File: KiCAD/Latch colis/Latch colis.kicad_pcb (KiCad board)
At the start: 2 copper layers, 140.8 x 44.7 mm, 12 parts, among them J1 KF301-2P, J2 KF301-2P, J3 KF301-2P, J4 Jauges, K1 Relay_SPDT, K2 Relay_SPDT, Q1 2N2222A, U1 Heltec_LoRa32_V2_RST_side, U2 Module HX711

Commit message: Passage au reveil par minuterie RTC, bibliotheques KiCad partagees, outils MCP
- Firmware courrier_emetteur : reveil profond par minuterie RTC au lieu du
  contact de porte, tarage HX711 persistant en memoire RTC, notification
  sans distinction nouveau/ancien courrier
- Variante "Latch colis sans inter" du schema KiCad, empreintes partagees
  (fp-lib-table) et PDF de brochage Heltec ajoutes
- Registre de travail (TODO.md) et espace de travail VS Code multi-dossiers
- Mise en place des serveurs MCP (Context7, Firecrawl, KiCad) avec script
  d'installation reutilisable sur une nouvelle machine (MCP-SETUP.md,
  setup-mcp-tools.ps1)

Co-Authored-By: Claude Sonnet 5 <noreply@anthropic.com>
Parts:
- Q1: footprint Package_TO_SOT_THT:TO-92 -> Package_TO_SOT_THT:TO-92L_Inline_Wide
- R1: value R -> 1k
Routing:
- net GND: track 166.6 -> 169.5 mm
- net Net-(Q1-Pad2): track 6.14 -> 8.73 mm
- net Net-(D1-K): track 189.7 -> 191.4 mm
- net Net-(U1-13): track 39.3 -> 41.0 mm
- net Net-(J2-Pad1): track 37.5 -> 36.3 mm
- net Net-(U1-33): track 71.9 -> 70.9 mm
- net Net-(J4-Pin_5): track 4.29 -> 5.25 mm
- net Net-(J4-Pin_3): track 4.29 -> 5.25 mm
- net Net-(J4-Pin_4): track 4.29 -> 5.25 mm
- net Net-(J4-Pin_2): track 4.29 -> 5.25 mm
- net Net-(J4-Pin_6): track 4.29 -> 5.25 mm
- net Net-(J4-Pin_1): track 4.29 -> 5.25 mm
- net Net-(D2-A): track 61.6 -> 62.2 mm
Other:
- board size 140.8 x 44.7 mm -> 150 x 50 mm

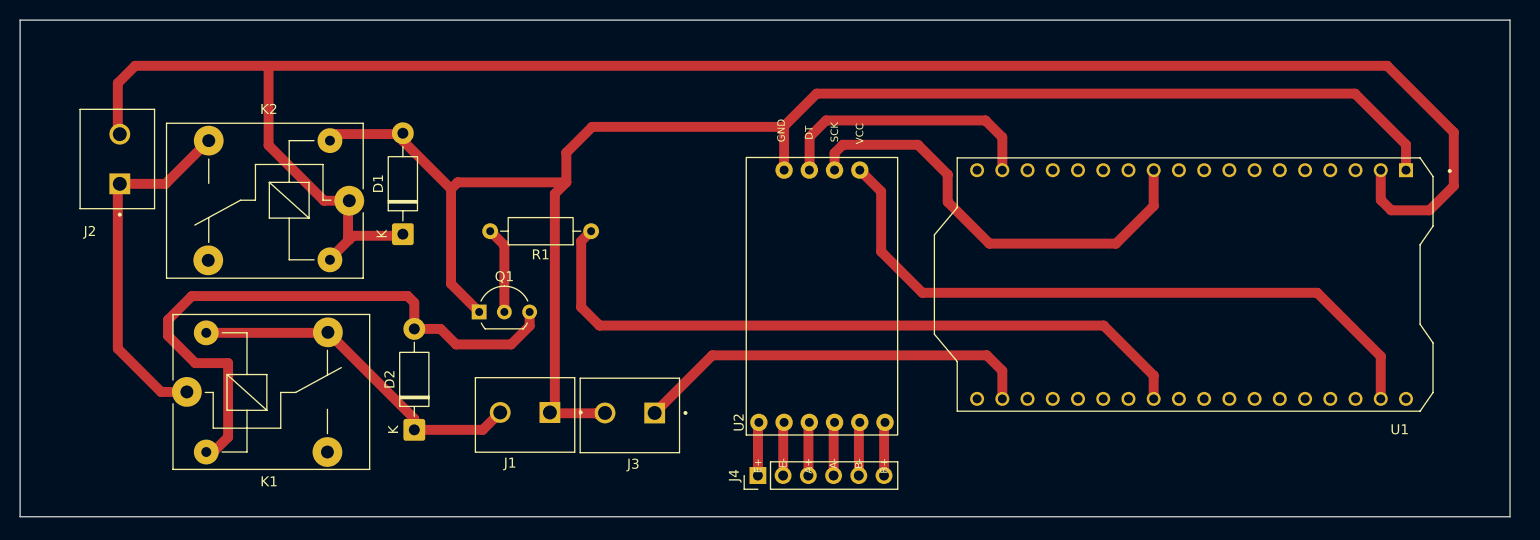
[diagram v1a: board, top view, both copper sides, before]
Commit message: Fusion boite-aux-lettres-lora : ajout docs, photos, variantes KiCad, binaires de test
- Docs/ : plan cotes boîte aux lettres, pinout Heltec, datasheet jauge 50kg, référence latch
- KiCAD : 4 variantes schémas latch MOSFET (v1, NE555, avec_lora, RS) + images références
- KiCAD Latch colis : fichiers PCB/SCH mis à jour (09-11/09), gravure actualisée
- KiCAD Symboles : bibliothèque Heltec LoRa32 V2
- src/bin : emetteur_test_1s, recepteur_test_1s, test_hx711
- src/archive : historique des premières versions emetteur/recepteur
- html/ : calculateurs (circuit verrouillage, échelle dBm, ping vs reçus)
- Lightburn : fichiers gravure laser (.lbrn2, .cwprj)
- .cargo/config.toml : target-dir + CARGO_WORKSPACE_DIR (fix embuild remote_component)
- Boîte aux lettres.md : documentation technique projet

Co-Authored-By: Claude Sonnet 4.6 <noreply@anthropic.com>
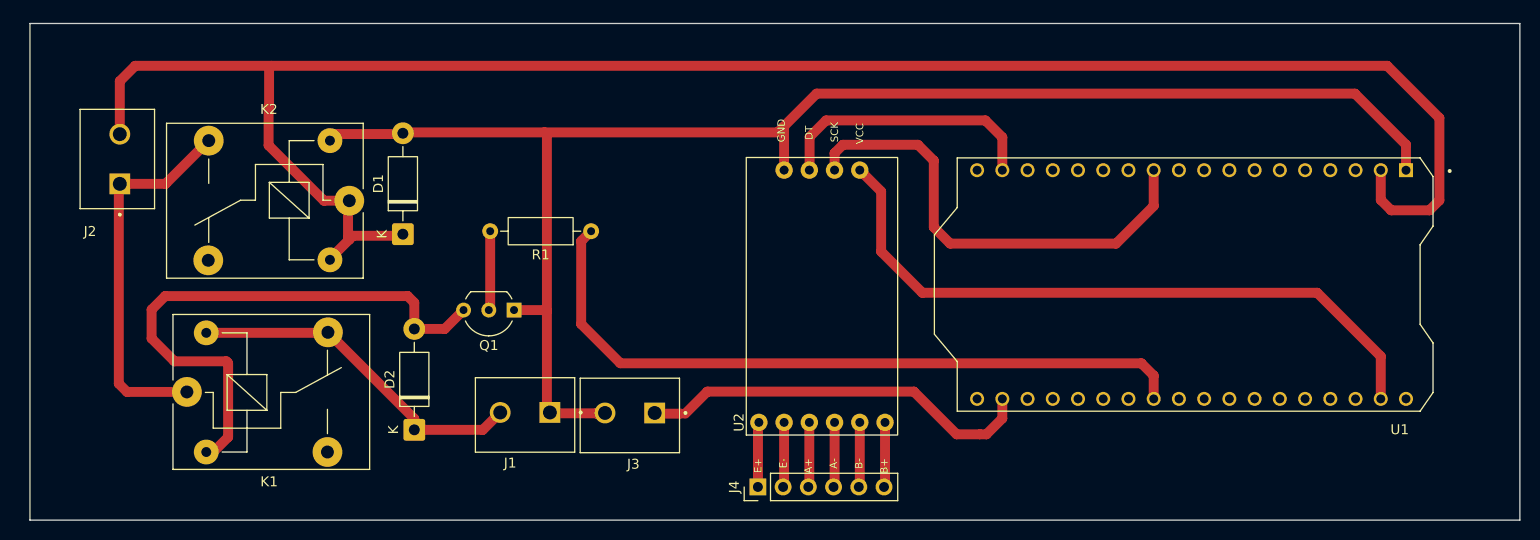
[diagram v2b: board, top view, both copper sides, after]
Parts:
- Q1: footprint Package_TO_SOT_THT:TO-92L_Inline_Wide -> Package_TO_SOT_THT:TO-92_Inline_Wide
- moved Q1 3.52 mm to (84.9, 64.4), turned to 180 degrees
- moved J4 1.15 mm to (109.4, 82.2)
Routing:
- net GND: track 169.5 -> 157.0 mm
- net Net-(D2-A): track 62.2 -> 57.6 mm
- net /SCK: track 45.1 -> 47.4 mm
- net Net-(J2-Pad1): track 36.3 -> 38.2 mm
- net Net-(D1-K): track 191.4 -> 190.1 mm
- net Net-(J4-Pin_5): track 5.25 -> 6.54 mm
- net Net-(J4-Pin_3): track 5.25 -> 6.54 mm
- net Net-(J4-Pin_4): track 5.25 -> 6.54 mm
- net Net-(J4-Pin_2): track 5.25 -> 6.54 mm
- net Net-(J4-Pin_6): track 5.25 -> 6.54 mm
- net Net-(J4-Pin_1): track 5.25 -> 6.40 mm
- net Net-(U1-13): track 41.0 -> 40.0 mm
- net Net-(U1-33): track 70.9 -> 71.9 mm
- net Net-(Q1-Pad2): track 8.73 -> 8.00 mm
